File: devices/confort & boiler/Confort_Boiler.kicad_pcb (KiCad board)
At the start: 2 copper layers, 16 parts, among them K1 DHT1, K2 DHT2, K3 DS18B20, P1 TOBOILER, P2 BOILERSW, U1 OPTO-TRANSISTOR4, U2 ARDUINO_MINI, U3 ENC28J60

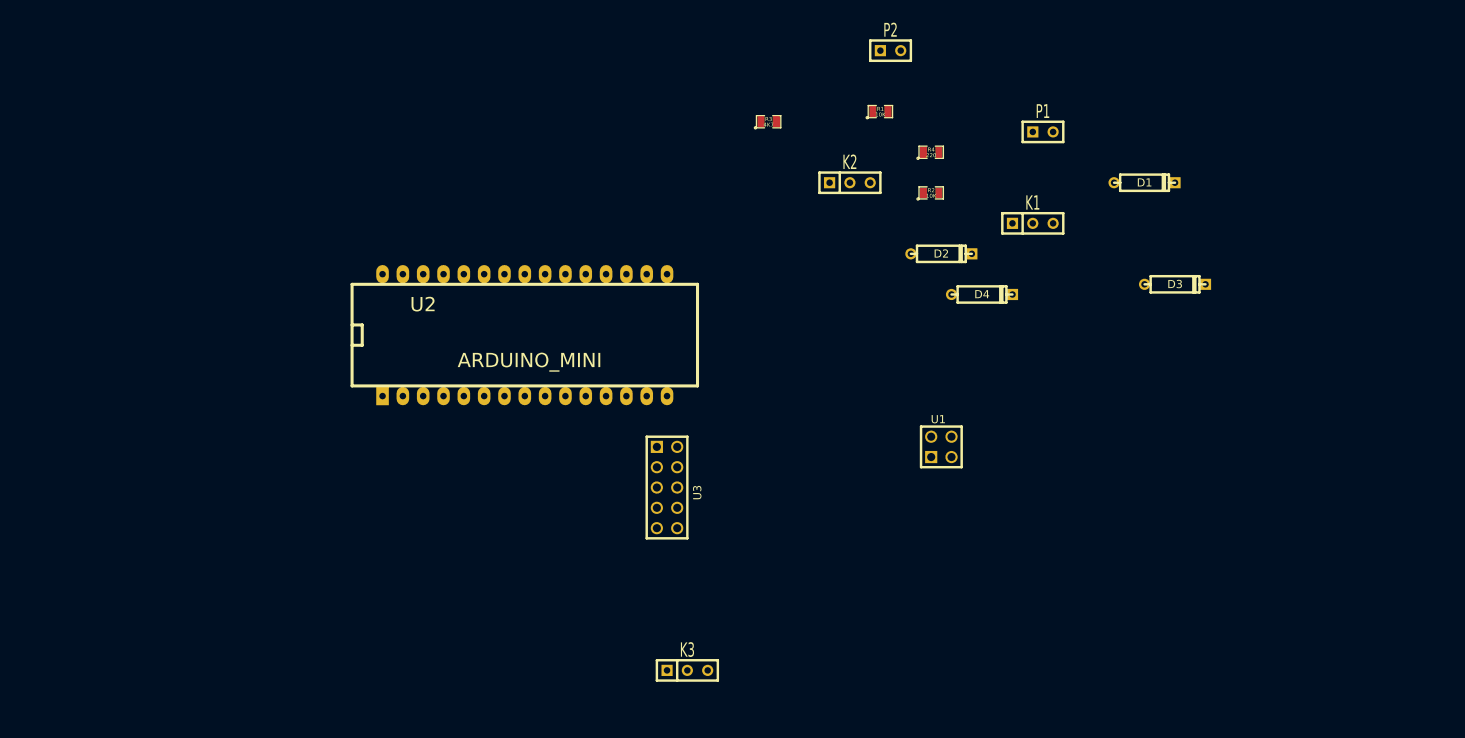
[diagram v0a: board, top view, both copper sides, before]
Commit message: modified the boiler schema in order to use Open Therm
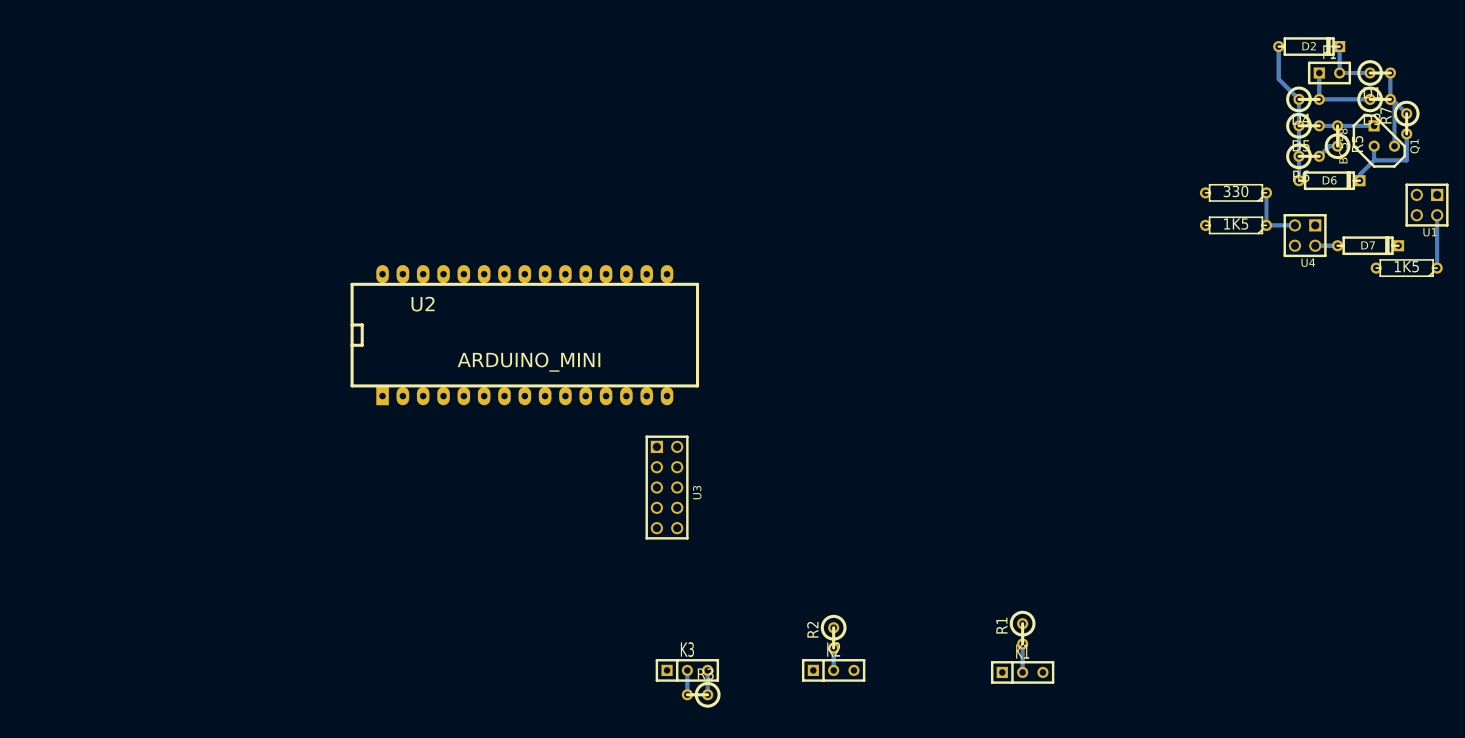
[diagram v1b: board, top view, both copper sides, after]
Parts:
- removed P2: BOILERSW, SIL-2
- added D5: 4v7, R1, F.Cu at (188.2, 28.4)
- added D6: 15V, D3, F.Cu at (190.8, 35.3)
- added D7: 4v3, D3, F.Cu at (195.6, 43.4)
- added Q1: BC558, TO92, F.Cu at (197.6, 29.7)
- added R5: 200, R1, F.Cu at (191.8, 29.7)
- added R6: 100, R1, F.Cu at (188.2, 32.3)
- added R7: 330, R1, F.Cu at (200.4, 28.2)
- added R8: 1K5, R3, F.Cu at (179.1, 40.9)
- added R9: 1K5, R3, F.Cu at (200.4, 46.2)
- added U4: OPTO-TRANSISTOR4, PIN_ARRAY_2X2, F.Cu at (187.7, 42.2)
- D1, D3, D4: footprint D3 -> R1
- R1, R2, R3: footprint SM0805 -> R1
- R4: value 220 -> 330; footprint SM0805 -> R3
- moved R3 72.2 mm to (111.8, 99.6), turned to 180 degrees
- moved U1 67.8 mm to (202.9, 38.4), turned to 180 degrees
- moved R1 67.7 mm to (152.4, 91.9), turned to 270 degrees
- moved K2 61.0 mm to (128.8, 96.5)
- moved R2 56.9 mm to (128.8, 92.5), turned to 270 degrees
- moved K1 56.1 mm to (152.4, 96.8)
- moved D2 52.8 mm to (188.2, 18.5)
- moved D4 47.6 mm to (188.2, 25.1)
- moved R4 38.4 mm to (179.1, 36.8), turned to 180 degrees
- moved P1 36.6 mm to (190.8, 21.8)
- moved D3 34.5 mm to (197.1, 25.1)
- moved D1 32.5 mm to (197.1, 21.8)
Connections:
- D1 pad 2: N-0000029 -> N-0000024
- D2 pad 1: N-0000030 -> N-0000025
- D3 pad 2: N-0000029 -> N-0000024
- D4 pad 1: N-0000030 -> N-0000025
- R4 pad 1: N-0000036 -> N-0000017
- R4 pad 2: LBOILER -> GND
- U1 pad 1: N-0000036 -> VCC
- U1 pad 2: GND -> N-0000018
- U1 pad 3: N-0000029 -> N-0000015
- U1 pad 4: N-0000030 -> N-0000027
- U2 pad 21: (no net) -> LRX
- U2 pad 23: (no net) -> LTX
- U2 pad 27: LBOILER -> (no net)
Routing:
- net N-0000025: track 0.00 -> 20.6 mm
- net N-0000027: track 0.00 -> 12.4 mm
- net N-0000024: track 0.00 -> 12.1 mm
- net N-0000019: track 0.00 -> 9.65 mm
- net N-0000017: track 0.00 -> 7.62 mm
- net N-000007: track 0.00 -> 7.11 mm
- net N-0000026: track 0.00 -> 6.86 mm
- net N-0000018: track 0.00 -> 6.60 mm
- net N-000008: track 0.00 -> 3.56 mm
- net VCC: track 0.00 -> 3.05 mm
- net LDS18B20: track 0.00 -> 3.05 mm
- net N-0000016: track 0.00 -> 2.81 mm
- net N-0000011: track 0.00 -> 2.79 mm
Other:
- net class Default: trace_width 0.254 -> 0.512; via_dia 0.889 -> 1.8

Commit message: pcb for boiler almost done
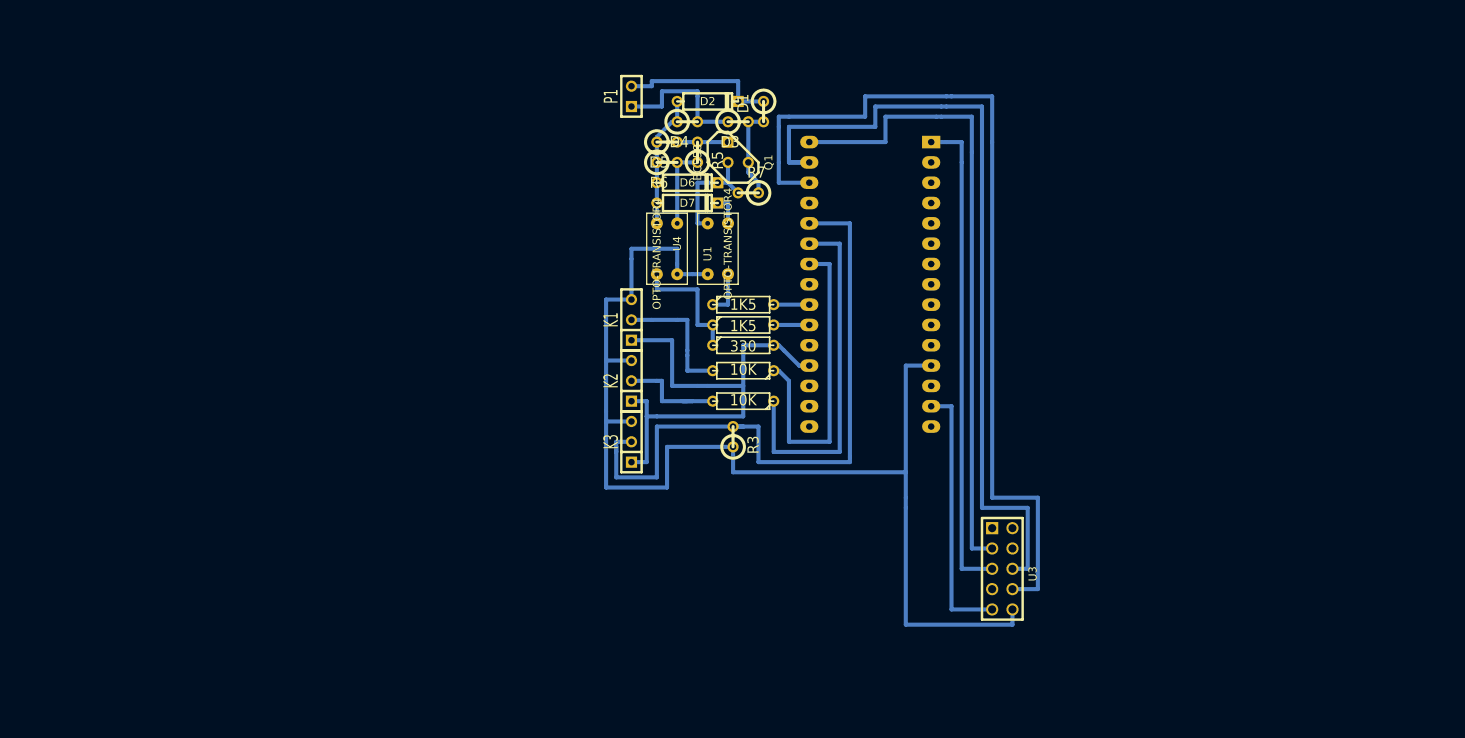
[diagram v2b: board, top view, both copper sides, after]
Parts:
- R1, R2: footprint R1 -> R3
- U1, U4: footprint PIN_ARRAY_2X2 -> PC817
- U2: moved to B.Cu
- moved U1 88.8 mm to (114.3, 43.2), turned to 90 degrees
- moved P1 87.3 mm to (103.5, 24.8), turned to 90 degrees
- moved D7 85.3 mm to (110.5, 38.1)
- moved R9 83.1 mm to (117.5, 50.8), turned to 0 degrees
- moved R7 82.7 mm to (118.1, 36.8), turned to 180 degrees
- moved Q1 80.8 mm to (116.8, 31.8)
- moved D3 80.3 mm to (116.8, 27.9)
- moved D5 80.3 mm to (108.0, 30.5)
- moved R6 80.3 mm to (108.0, 33.0)
- moved D6 80.3 mm to (110.5, 35.6)
- moved R5 80.0 mm to (111.8, 31.8)
- moved U4 79.8 mm to (108.0, 44.5), turned to 270 degrees
- moved D4 77.8 mm to (110.5, 27.9)
- moved D1 77.2 mm to (120.0, 26.7), turned to 270 degrees
- moved D2 75.5 mm to (113.0, 25.4)
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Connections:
- U2 pad 13: N-0000023 (its old number) -> (no net)
- U2 pad 2: N-000009 (its old number) -> (no net)
- U2 pad 20: N-0000022 (its old number) -> (no net)
- U2 pad 22: (no net) -> LTX
- U2 pad 23: LTX -> (no net)
- U3 pad 1: N-0000022 (its old number) -> (no net)
- U3 pad 10: N-000009 (its old number) -> VCC
- U3 pad 7: N-0000023 (its old number) -> (no net)
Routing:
- net VCC: track 3.05 -> 148.6 mm
- net N-000002: track 0.00 -> 111.8 mm
- net N-000003: track 0.00 -> 101.6 mm
- net GND: track 0.00 -> 94.4 mm
- net LDS18B20: track 3.05 -> 83.2 mm
- net N-000004: track 0.00 -> 80.0 mm
- net N-000005: track 0.00 -> 61.0 mm
- net LDHT2: track 0.00 -> 44.4 mm
- net LDHT1: track 0.00 -> 39.9 mm
- net N-0000010: track 3.56 -> 16.5 mm
- net N-000009: track 7.11 -> 19.7 mm
- net N-0000013: track 2.79 -> 14.6 mm
- net N-0000016: track 7.62 -> 15.9 mm
- net N-0000019: track 9.65 -> 17.8 mm
- net N-0000017: track 2.81 -> 10.2 mm
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
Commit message: finished with pcb
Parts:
- K1, K2, K3: footprint SIL-3 -> DG306-5.08-03
- P1: footprint SIL-2 -> DG306-5.08-02
- R8, R9: footprint R3 -> R1
- moved K1 17.6 mm to (99.7, 35.6)
- moved K2 10.3 mm to (99.7, 50.8)
- moved U1 5.85 mm to (120.0, 44.5)
- moved U4 5.24 mm to (113.0, 45.7)
- moved R3 5.12 mm to (113.7, 71.8)
- moved P1 4.26 mm to (99.7, 22.9)
- moved K3 4.26 mm to (99.7, 66.0)
- moved R9 3.24 mm to (120.7, 51.4)
- moved R8 3.17 mm to (114.9, 51.4)
- moved U3 1.27 mm to (149.9, 85.1)
- moved R2 0.64 mm to (117.5, 62.2)
- moved R1 0.63 mm to (117.5, 59.7)
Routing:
- net VCC: track 148.6 -> 254.0 mm
- net GND: track 94.4 -> 116.2 mm
- net N-0000010: track 16.5 -> 38.1 mm
- net LDS18B20: track 83.2 -> 70.5 mm
- net N-0000023: track 14.5 -> 26.0 mm
- net LRX: track 4.45 -> 15.9 mm
- net N-0000013: track 14.6 -> 25.4 mm
- net N-0000018: track 3.81 -> 10.8 mm
- net N-0000022: track 16.7 -> 23.0 mm
- net N-0000016: track 15.9 -> 9.53 mm
- net N-000009: track 19.7 -> 25.4 mm
- net N-0000017: track 10.2 -> 15.2 mm
- net N-0000019: track 17.8 -> 22.2 mm
- net N-000003: track 101.6 -> 104.8 mm
- net LTX: track 4.45 -> 6.61 mm
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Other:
- board outline added: 62.2 x 78.1 mm
- board text added: "OpenTherm 1.0 @2015"

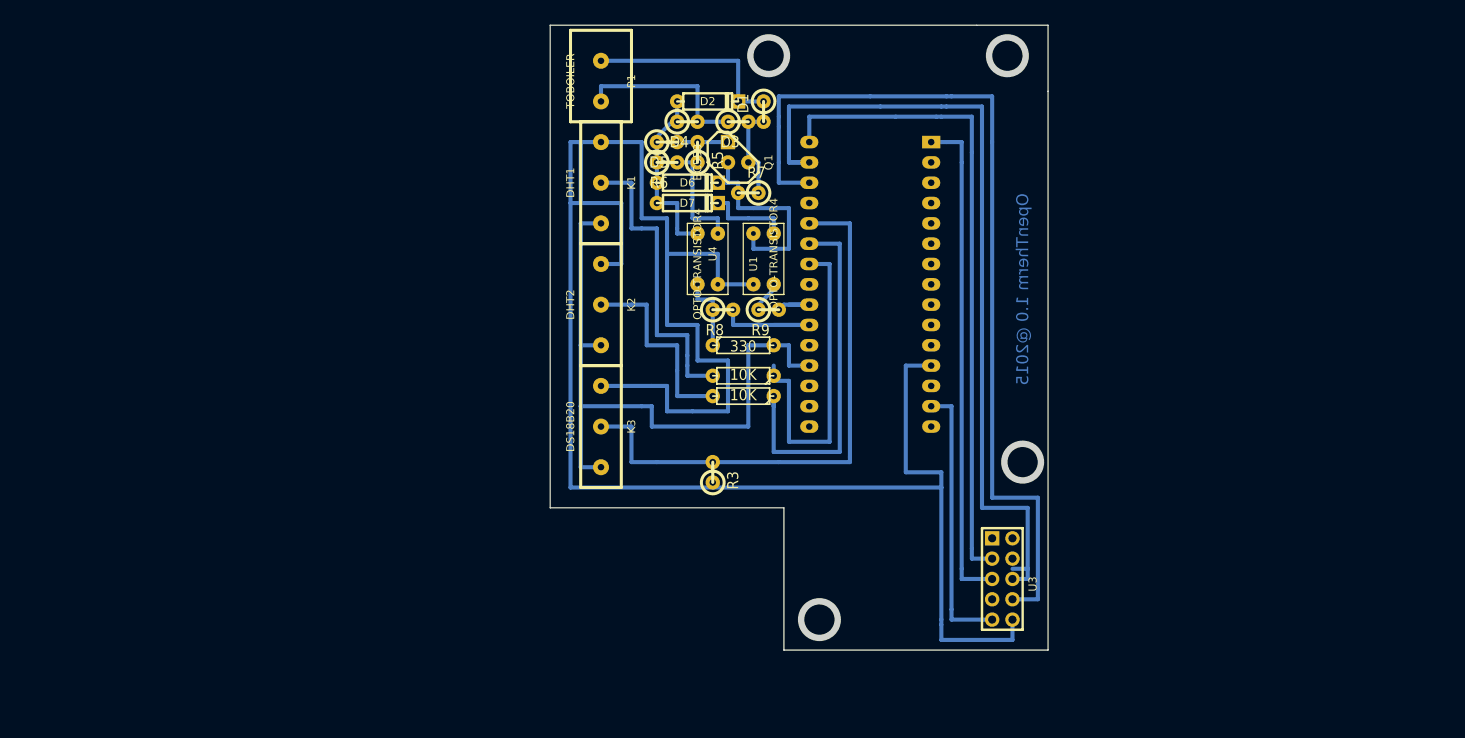
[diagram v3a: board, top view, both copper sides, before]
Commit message: checked the pcb with real components and made according adjusments
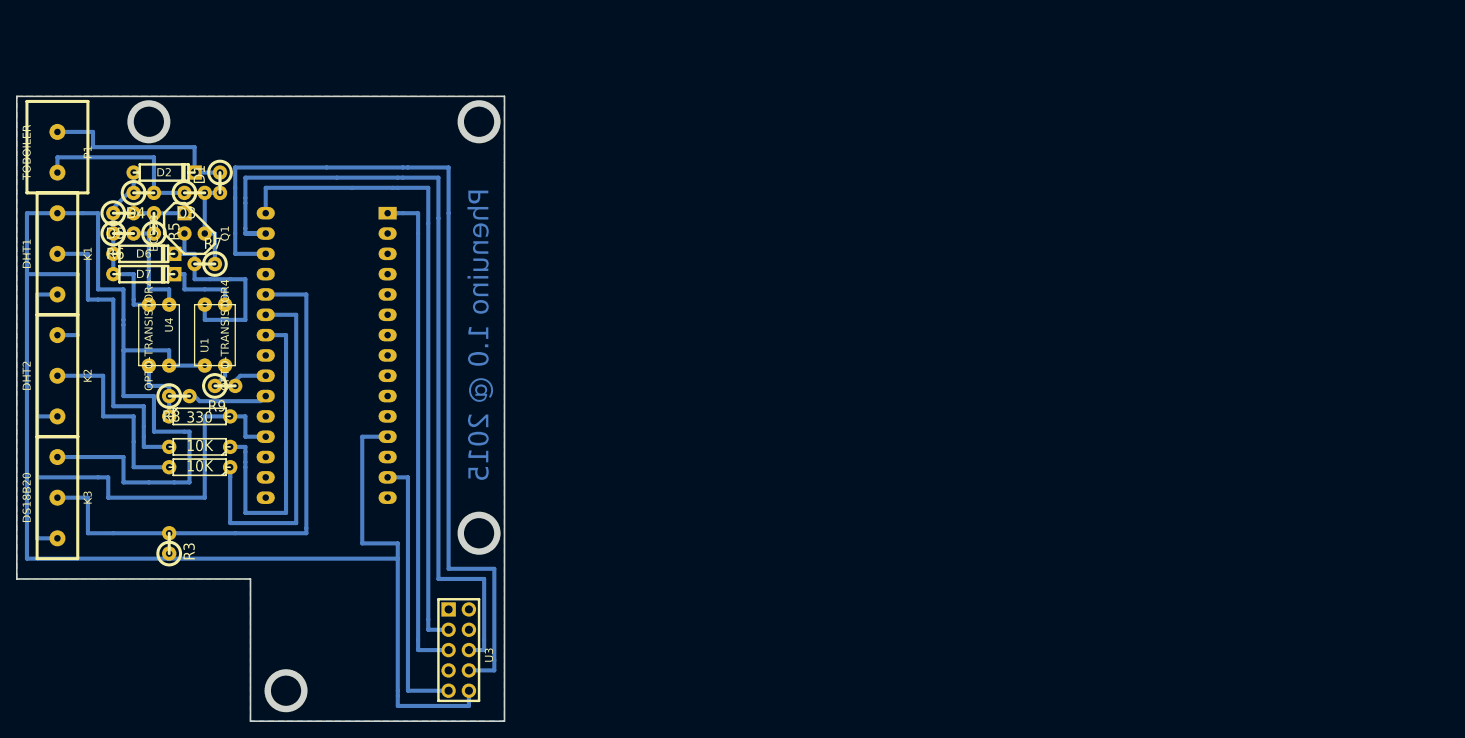
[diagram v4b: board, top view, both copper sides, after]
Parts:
- moved U1 69.3 mm to (51.4, 54.6)
- moved U4 69.2 mm to (44.5, 54.6)
- moved R8 68.8 mm to (47.0, 62.2)
- moved R9 68.6 mm to (52.7, 61.0)
- moved R3 68.5 mm to (45.7, 80.6)
- moved R5 68.5 mm to (43.8, 40.6)
- moved U3 68.5 mm to (81.9, 94.0)
- moved D1 68.5 mm to (52.1, 35.6)
- moved D2 68.5 mm to (45.1, 34.3)
- moved D3 68.5 mm to (48.9, 36.8)
- moved D4 68.5 mm to (42.5, 36.8)
- moved D5 68.5 mm to (40.0, 39.4)
- moved D6 68.5 mm to (42.5, 44.5)
- moved D7 68.5 mm to (42.5, 47.0)
- moved K1 68.5 mm to (31.8, 44.5)
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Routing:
- net LRX: track 15.9 -> 10.1 mm
- net VCC: track 254.0 -> 251.5 mm
- net LTX: track 6.61 -> 4.71 mm
- net N-000003: track 104.8 -> 102.9 mm
- net LDHT1: track 41.3 -> 40.0 mm
- net N-000007: track 3.96 -> 3.07 mm
- net N-0000023: track 26.0 -> 26.7 mm
- net N-0000016: track 9.53 -> 8.89 mm
- net N-0000017: track 15.2 -> 14.6 mm
- net N-0000022: track 23.0 -> 22.4 mm
- net N-0000018: track 10.8 -> 10.2 mm
- added copper zone on B.Cu, net (none)
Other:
- board size 62.2 x 78.1 mm -> 61 x 78.1 mm
- board text added: "Phenuino 1.0 @ 2015"
- board text removed: "OpenTherm 1.0 @2015"
